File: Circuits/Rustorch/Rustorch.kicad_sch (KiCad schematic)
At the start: 57 parts, among them CN1 USB_C_Receptacle_USB2.0_16P, CN2 OLED_128x64_IIC, Q1 2SC1815, Q2 2SC1815, Q3 2SC1815, Q4 2SC1815, SW1 SW_POWER (5P), SW2 RESET, SW3 SW_BOOT, SW4 SW_UP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

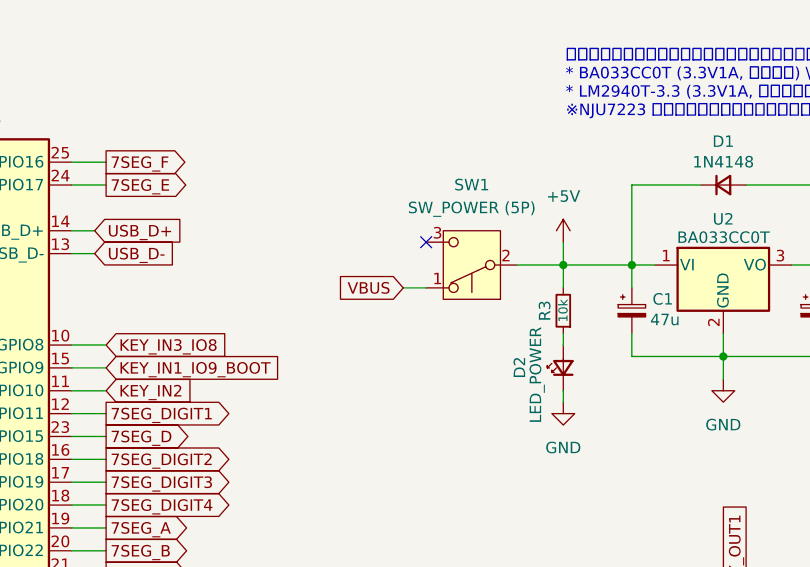
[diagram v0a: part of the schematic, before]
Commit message: (Rustorch) 基板の電源スイッチを修正
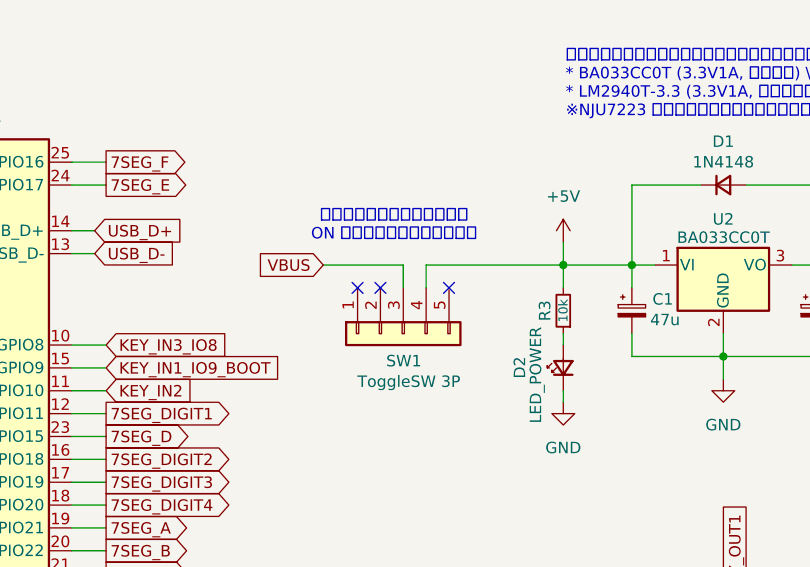
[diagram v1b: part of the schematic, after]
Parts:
- removed SW1: SW_POWER (5P), Button_Switch_THT:SW_Slide_SPDT_Straight_CK_OS102011MS2Q, symbol Switch:SW_Push_SPDT
- added SW1: ToggleSW 3P, Connector_PinSocket_2.54mm:PinSocket_1x05_P2.54mm_Vertical, symbol Connector_Generic:Conn_01x05
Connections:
- net +5V: now also SW1.4 (Pin_4)
- net VBUS: now also SW1.3 (Pin_3)
- no-connect marks 3 -> 5
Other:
- note added: "スイッチを上に押したときに ON になるようにピン配置した"
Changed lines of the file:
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@@
 	)
 	(no_connect
-		(at 210.82 45.72)
+		(at 203.2 50.8)
+	)
+	(no_connect
+		(at 205.74 50.8)
+	)
+	(no_connect
+		(at 213.36 50.8)
 	)
 	(bus_entry
@@
 	(wire
 		(pts
+			(xy 208.28 48.26) (xy 208.28 50.8)
+		)
+		(stroke
+			(width 0)
+			(type default)
+		)
+	)
+	(wire
+		(pts
 			(xy 66.04 149.86) (xy 68.58 149.86)
 		)
@@
 	(wire
 		(pts
-			(xy 220.98 48.26) (xy 226.06 48.26)
-		)
-		(stroke
-			(width 0)
-			(type default)
-		)
-	)
-	(wire
-		(pts
 			(xy 262.89 86.36) (xy 262.89 88.9)
 		)
@@
 	(wire
 		(pts
-			(xy 36.83 172.72) (xy 46.99 172.72)
+			(xy 199.39 48.26) (xy 208.28 48.26)
 		)
 		(stroke
@@
 	(wire
 		(pts
-			(xy 261.62 48.26) (xy 261.62 50.8)
+			(xy 36.83 172.72) (xy 46.99 172.72)
 		)
 		(stroke
@@
 	(wire
 		(pts
-			(xy 93.98 58.42) (xy 93.98 64.77)
+			(xy 261.62 48.26) (xy 261.62 50.8)
 		)
 		(stroke
@@
 	(wire
 		(pts
-			(xy 88.9 149.86) (xy 91.44 149.86)
+			(xy 93.98 58.42) (xy 93.98 64.77)
 		)
 		(stroke
@@
 	(wire
 		(pts
-			(xy 83.82 147.32) (xy 83.82 149.86)
+			(xy 88.9 149.86) (xy 91.44 149.86)
 		)
 		(stroke
@@
 	(wire
 		(pts
-			(xy 245.11 97.79) (xy 250.19 97.79)
+			(xy 83.82 147.32) (xy 83.82 149.86)
 		)
 		(stroke
@@
 	(wire
 		(pts
-			(xy 208.28 50.8) (xy 210.82 50.8)
+			(xy 245.11 97.79) (xy 250.19 97.79)
 		)
 		(stroke
@@
 	(wire
 		(pts
+			(xy 210.82 48.26) (xy 226.06 48.26)
+		)
+		(stroke
+			(width 0)
+			(type default)
+		)
+	)
+	(wire
+		(pts
 			(xy 171.45 74.93) (xy 175.26 74.93)
 		)
@@
 	(wire
 		(pts
+			(xy 210.82 50.8) (xy 210.82 48.26)
+		)
+		(stroke
+			(width 0)
+			(type default)
+		)
+	)
+	(wire
+		(pts
 			(xy 93.98 50.8) (xy 91.44 50.8)
 		)
@@
 		)
 	)
+	(text "スイッチを上に押したときに\nON になるようにピン配置した"
+		(exclude_from_sim no)
+		(at 207.264 43.942 0)
+		(effects
+			(font
+				(face "Meiryo UI")
+				(size 1.27 1.27)
+			)
+		)
+	)
 	(text "三端子レギュレータは以下のいずれかを使用する予定\n* BA033CC0T (3.3V1A, モールド) \\100\n* LM2940T-3.3 (3.3V1A, 非モールド) \\60\n※NJU7223 はピン配置が異なるので使用不可"
 		(exclude_from_sim no)
@@
 	(global_label "VBUS"
 		(shape input)
-		(at 208.28 50.8 180)
+		(at 199.39 48.26 180)
 		(fields_autoplaced yes)
 		(effects
@@
 		)
 		(property "Intersheetrefs" "${INTERSHEET_REFS}"
-			(at 200.3962 50.8 0)
+			(at 191.5062 48.26 0)
 			(effects
 				(font
@@
 	)
 	(symbol
-		(lib_id "Switch:SW_Push_SPDT")
-		(at 215.9 48.26 180)
-		(unit 1)
-		(exclude_from_sim no)
-		(in_bom yes)
-		(on_board yes)
-		(dnp no)
-		(fields_autoplaced yes)
-		(property "Reference" "SW1"
-			(at 215.9 39.37 0)
-			(effects
-				(font
-					(size 1.27 1.27)
-				)
-			)
-		)
-		(property "Value" "SW_POWER (5P)"
-			(at 215.9 41.91 0)
-			(effects
-				(font
-					(size 1.27 1.27)
-				)
-			)
-		)
-		(property "Footprint" "Button_Switch_THT:SW_Slide_SPDT_Straight_CK_OS102011MS2Q"
-			(at 215.9 48.26 0)
-			(effects
-				(font
-					(size 1.27 1.27)
-				)
-				(hide yes)
-			)
-		)
-		(property "Datasheet" "~"
-			(at 215.9 48.26 0)
-			(effects
-				(font
-					(size 1.27 1.27)
-				)
-				(hide yes)
-			)
-		)
-		(property "Description" "Momentary Switch, single pole double throw"
-			(at 215.9 48.26 0)
-			(effects
-				(font
-					(size 1.27 1.27)
-				)
-				(hide yes)
-			)
-		)
-		(pin "1"
-		)
-		(pin "2"
-		)
-		(pin "3"
-		)
-		(instances
-			(project ""
-				(path "/3b188497-bb0d-4776-a9fa-7cb2b780d2ff"
-					(reference "SW1")
-					(unit 1)
-				)
-			)
-		)
-	)
-	(symbol
 		(lib_id "Device:LED_Small")
 		(at 226.06 59.69 90)
@@
 					(unit 1)
 				)
+			)
+		)
+	)
+	(symbol
+		(lib_id "Connector_Generic:Conn_01x05")
+		(at 208.28 55.88 90)
+		(mirror x)
+		(unit 1)
+		(exclude_from_sim no)
+		(in_bom yes)
+		(on_board yes)
+		(dnp no)
+		(property "Reference" "SW1"
+			(at 210.312 58.928 90)
+			(effects
+				(font
+					(size 1.27 1.27)
+				)
+				(justify left)
+			)
+		)
+		(property "Value" "ToggleSW 3P"
+			(at 214.63 61.214 90)
+			(effects
+				(font
+					(size 1.27 1.27)
+				)
+				(justify left)
+			)
+		)
+		(property "Footprint" "Connector_PinSocket_2.54mm:PinSocket_1x05_P2.54mm_Vertical"
+			(at 208.28 55.88 0)
+			(effects
+				(font
+					(size 1.27 1.27)
+				)
+				(hide yes)
+			)
+		)
+		(property "Datasheet" "~"
+			(at 208.28 55.88 0)
+			(effects
+				(font
+					(size 1.27 1.27)
+				)
+				(hide yes)
+			)
+		)
+		(property "Description" "Generic connector, single row, 01x05, script generated (kicad-library-utils/schlib/autogen/connector/)"
+			(at 208.28 55.88 0)
+			(effects
+				(font
+					(size 1.27 1.27)
+				)
+				(hide yes)
+			)
+		)
+		(pin "5"
+		)
+		(pin "3"
+		)
+		(pin "1"
+		)
+		(pin "2"
+		)
+		(pin "4"
+		)
+		(instances
+			(project ""
+				(path "/3b188497-bb0d-4776-a9fa-7cb2b780d2ff"
+					(reference "SW1")
+					(unit 1)
+				)

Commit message: (Rustorch) 配線作業 (4層化)
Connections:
- net at Q4.2 (C), U6.3 (CC): no longer U6.8 (CC)
- net at Q3.2 (C), U5.3 (CC): no longer U5.8 (CC)
- net at Q1.2 (C), U3.3 (CC): no longer U3.8 (CC)
- net at Q2.2 (C), U4.3 (CC): no longer U4.8 (CC)
- no-connect marks 5 -> 9
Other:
- moved on the sheet: Q1, Q2, Q3, Q4
